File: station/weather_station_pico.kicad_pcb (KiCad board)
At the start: 2 copper layers, 60.2 x 74.1 mm, 26 parts, among them J1 Conn_01x03, J2 1984617, J3 STEMMA, J4 STEMMA_QT, J5 DS18B20, J6 1X7_HEADER, J7 73412-0110, J8 RJ11, J9 RJ11, U1 PICO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

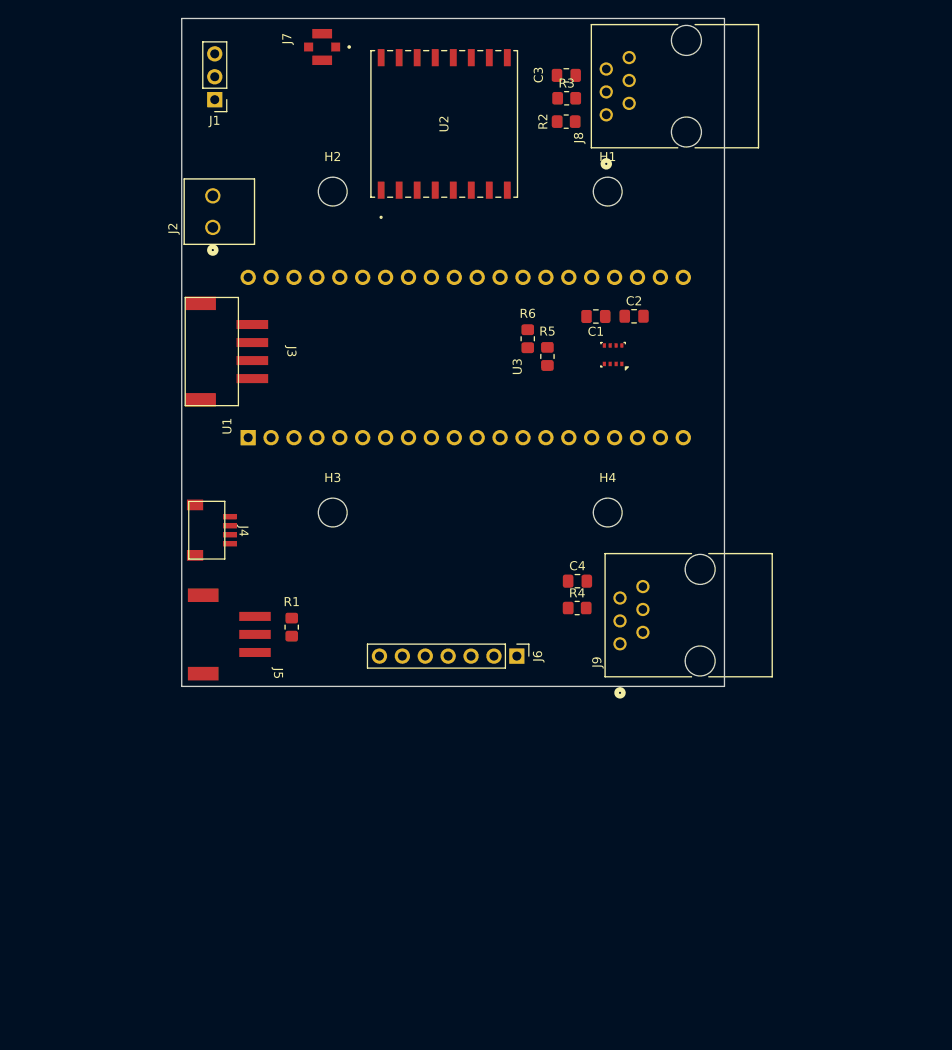
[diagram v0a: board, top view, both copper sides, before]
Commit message: Updated the weather stations components
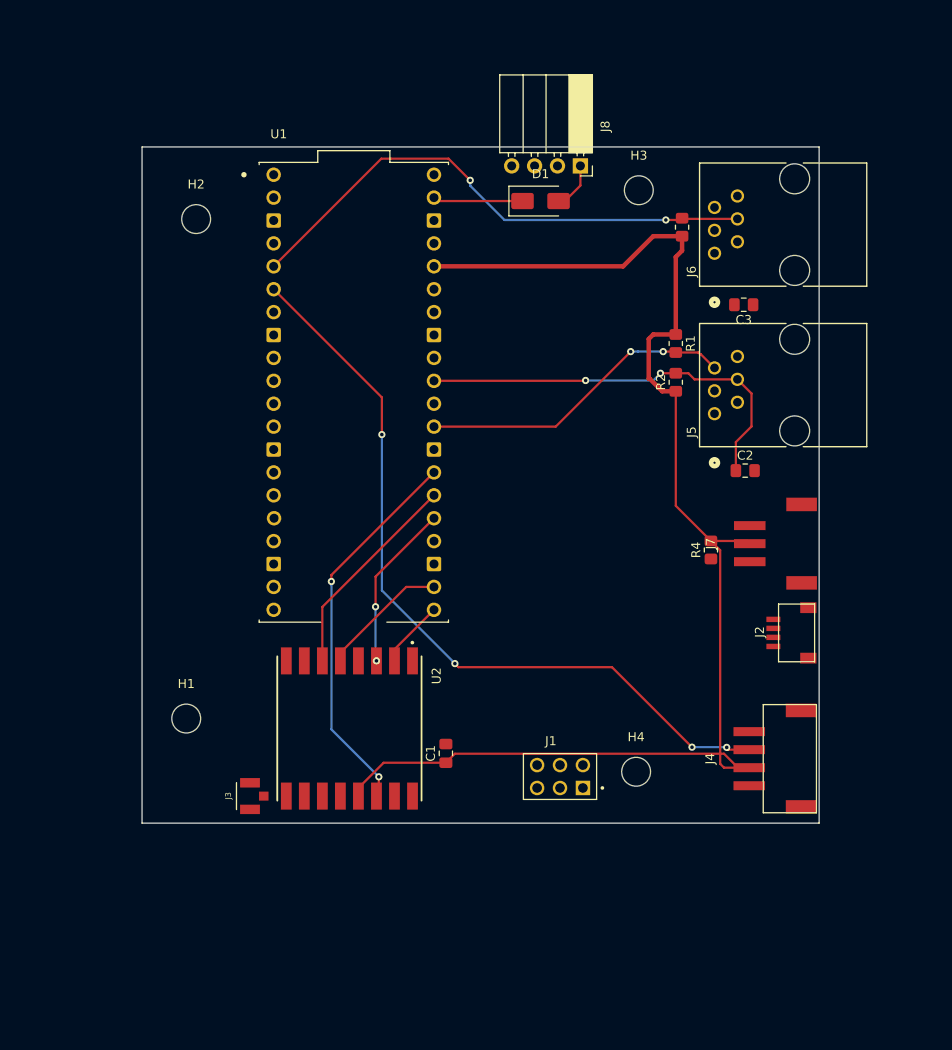
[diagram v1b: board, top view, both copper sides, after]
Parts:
- removed C4: 10pF, Capacitor_SMD:C_0805_2012Metric_Pad1.18x1.45mm_HandSolder
- removed J9: RJ11, WeatherStation:CONN6_5555165-1_TEC
- removed R5, R6: 4.7K, Resistor_SMD:R_0805_2012Metric_Pad1.20x1.40mm_HandSolder
- removed U3: BME280, Package_LGA:Bosch_LGA-8_2.5x2.5mm_P0.65mm_ClockwisePinNumbering
- added D1: SS12, Diode_SMD:D_SMA, F.Cu at (154.6, 65.5)
- C1: value 100nF -> 10uF
- C2: value 100nF -> 10pF
- J1: value Conn_01x03 -> DebugHeader; footprint Connector_PinHeader_2.54mm:PinHeader_1x03_P2.54mm_Vertical -> WeatherStation:DebugHeader
- J2: value 1984617 -> STEMMA_QT; footprint WeatherStation:CONN_1984617_PXC -> WeatherStation:STEMMA_SMALL
- J3: value STEMMA -> 73412-0110; footprint WeatherStation:STEMMA_LARGE -> WeatherStation:Antenna
- J4: value STEMMA_QT -> STEMMA; footprint WeatherStation:STEMMA_SMALL -> WeatherStation:STEMMA_LARGE
- J5: value DS18B20 -> RJ11; footprint WeatherStation:STEMMA_LARGE_3pin -> WeatherStation:CONN6_5555165-1_TEC
- J6: value 1X7_HEADER -> RJ11; footprint Connector_PinHeader_2.54mm:PinHeader_1x07_P2.54mm_Vertical -> WeatherStation:CONN6_5555165-1_TEC
- J7: value 73412-0110 -> DS18B20; footprint 734120110:MOLEX_73412-0110 -> WeatherStation:STEMMA_LARGE_3pin
- J8: value RJ11 -> Conn_01x04; footprint WeatherStation:CONN6_5555165-1_TEC -> Connector_PinSocket_2.54mm:PinSocket_1x04_P2.54mm_Horizontal
- R1: value R -> 10K
- R4: value 10K -> 4.7k
- U1: value PICO -> Pico; footprint WeatherStation:PinHeader_2x20_P2.54mm_Vertical -> WeatherStation:MODULE_SC918_PINS
- U2: footprint RFM69:RFM69HCW_SPK -> WeatherStation:RFM69
- moved J1 84.3 mm to (156.8, 129.3), turned to 0 degrees
- moved J2 77.4 mm to (181.2, 113.4)
- moved H1 74.8 mm to (115.3, 122.9)
- moved J7 73.8 mm to (179.6, 103.5)
- moved U2 67.9 mm to (133.4, 124.0), turned to -90 degrees
- moved J4 65.2 mm to (179.5, 127.3), turned to 90 degrees
- moved J5 58.1 mm to (173.9, 89.1), turned to 90 degrees
- moved R1 53.0 mm to (169.6, 81.3)
- moved C1 51.2 mm to (144.1, 126.8), turned to 90 degrees
- moved J6 49.8 mm to (173.9, 71.3), turned to 90 degrees
- moved J3 49.3 mm to (122.4, 131.5), turned to 90 degrees
- moved H3 49.3 mm to (165.5, 64.3)
- moved C3 32.2 mm to (177.1, 77.0)
- moved R2 31.4 mm to (169.6, 85.6), turned to 90 degrees
- moved H4 28.9 mm to (165.2, 128.8)
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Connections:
- net /RFM69_CS renamed /RFM69 Radio/RFM69_CS
- net /RFM69_RESET renamed /RFM69 Radio/RFM69_RESET
- net /SPI0_CLK renamed /RFM69 Radio/RFM69_CLK
- net /SPI0_MISO renamed /RFM69 Radio/RFM69_MISO
- net /SPI0_MOSI renamed /RFM69 Radio/RFM69_MOSI
- net /UART_TX renamed /UART0_TX
- C1 pad 1: VCC -> +3.3V
- C2 pad 1: VCC -> /WINDSPEED_TGR
- C3 pad 1: /WINDSPEED_TGR -> /RAIN_COUNT
- J1 pad 2: /UART_RX -> /SWCLK
- J1 pad 3: GND -> /UART0_RX
- J2 pad 2: +5V -> +3.3V
- J3 pad 1: GND -> Net-(U2-ANT)
- J3 pad 2: VCC -> GND
- J3 pad 3: /SDA -> (no net)
- J4 pad 2: VCC -> +3.3V
- J4 pad 3: /SDA -> /I2C0_SDA
- J4 pad 4: /SCL -> /I2C0_SCL
- J5 pad 1: /ONE_WIRE -> unconnected-(J5-Pad1)
- J5 pad 2: VCC -> GND
- J5 pad 4: (no net) -> /WINDSPEED_TGR
- J5 pad 5: (no net) -> /WINDDIR_OUT
- J6 pad 1: /MOSI -> unconnected-(J6-Pad1)
- J6 pad 2: /MISO -> unconnected-(J6-Pad2)
- J6 pad 3: /SCK -> GND
- J6 pad 4: /~{CS} -> /RAIN_COUNT
- J6 pad 5: /LIGHTNING_INT -> unconnected-(J6-Pad5)
- J6 pad 6: VCC -> unconnected-(J6-Pad6)
- J7 pad 1: Net-(U2-ANT) -> /ONE_WIRE
- J7 pad 2: GND -> +3.3V
- J7 pad 3: (no net) -> GND
- J8 pad 1: unconnected-(J8-Pad1) -> /Battery Charger/VOUT
- J8 pad 2: GND -> /Battery Charger/SET
- J8 pad 3: GND -> /Battery Charger/~{FAULT}
- J8 pad 4: /WINDSPEED_TGR -> /Battery Charger/~{CHRG}
- R1 pad 1: /ONE_WIRE -> +3.3V
- R1 pad 2: VCC -> /WINDDIR_OUT
- R2 pad 1: VCC -> +3.3V
- R2 pad 2: /WINDDIR_OUT -> /WINDSPEED_TGR
- R3 pad 1: VCC -> +3.3V
- R3 pad 2: /WINDSPEED_TGR -> /RAIN_COUNT
- R4 pad 1: VCC -> /ONE_WIRE
- R4 pad 2: /RAIN_COUNT -> +3.3V
- U1 pad 16: /SDA -> unconnected-(U1-GP12-Pad16)
- U1 pad 17: /SCL -> unconnected-(U1-GP13-Pad17)
- U1 pad 2: /UART_RX -> /UART0_RX
- U1 pad 20: /ONE_WIRE -> unconnected-(U1-GP15-Pad20)
- U1 pad 27: /FRM69_INTR -> /RFM69 Radio/RFM69_INTR
- U1 pad 29: /WINDSPEED_TGR -> /WINDDIR_OUT
- U1 pad 31: /WINDDIR_OUT -> /WINDSPEED_TGR
- U1 pad 36: VCC -> +3.3V
- U1 pad 39: +5V -> Net-(D1-K)
- U1 pad 5: unconnected-(U1-GP3-Pad5) -> /RAIN_COUNT
- U1 pad 6: /RAIN_COUNT -> /I2C0_SDA
- U1 pad 7: unconnected-(U1-GP5-Pad7) -> /I2C0_SCL
- U2 pad 13: VCC -> +3.3V
- U2 pad 14: /RFM69_INTR -> /RFM69 Radio/RFM69_INTR
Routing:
- net +3.3V: track 0.00 -> 148.9 mm
- net /I2C0_SDA: track 0.00 -> 86.5 mm, vias 0 -> 4
- net /RAIN_COUNT: track 0.00 -> 59.7 mm, vias 0 -> 2
- net /WINDSPEED_TGR: track 0.00 -> 45.8 mm, vias 0 -> 2
- net /RFM69 Radio/RFM69_INTR: track 0.00 -> 42.9 mm, vias 0 -> 2
- net /WINDDIR_OUT: track 0.00 -> 35.3 mm, vias 0 -> 2
- net /RFM69 Radio/RFM69_RESET: track 0.00 -> 23.5 mm
- net /RFM69 Radio/RFM69_MOSI: track 0.00 -> 18.5 mm, vias 0 -> 2
- net /RFM69 Radio/RFM69_CS: track 0.00 -> 14.3 mm
- net Net-(D1-K): track 0.00 -> 9.98 mm
- net /RFM69 Radio/RFM69_MISO: track 0.00 -> 7.47 mm
- net /Battery Charger/VOUT: track 0.00 -> 5.31 mm
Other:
- board size 60.2 x 74.1 mm -> 75.1 x 75 mm

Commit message: Signed-off-by: Scott Perkins <whatisbyandby@gmail.com>
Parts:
- J8: value Conn_01x04 -> Battery Charger; footprint Connector_PinSocket_2.54mm:PinSocket_1x04_P2.54mm_Horizontal -> Connector_PinSocket_2.54mm:PinSocket_2x03_P2.54mm_Vertical
- U1: footprint WeatherStation:MODULE_SC918_PINS -> WeatherStation:Pico_SMD_Headers; moved to B.Cu
- moved H3 63.9 mm to (117.2, 106.2)
- moved H1 58.5 mm to (117.3, 64.4)
- moved H2 42.9 mm to (159.1, 64.3)
- moved H4 23.6 mm to (159.1, 106.0)
- moved J8 9.14 mm to (166.6, 66.7), turned to 180 degrees
- moved J3 9.12 mm to (113.7, 128.8)
- moved U2 8.70 mm to (124.7, 124.1)
- moved C1 8.70 mm to (135.4, 126.8)
- moved R3 5.63 mm to (170.1, 74.0)
- moved D1 4.49 mm to (155.0, 70.0)
- moved U1 4.44 mm to (138.0, 88.3), turned to 180 degrees
- moved J4 4.30 mm to (179.4, 123.0)
- moved J7 3.04 mm to (179.6, 100.5)
- moved C2 2.84 mm to (177.7, 92.6)
- moved R4 2.60 mm to (173.6, 101.6)
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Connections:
- net /Battery Charger/VOUT renamed /Battery Charger/Load+
- J8 pad 2: /Battery Charger/SET -> GND
- J8 pad 3: /Battery Charger/~{FAULT} -> GND
- J8 pad 4: /Battery Charger/~{CHRG} -> /Battery Charger/SET
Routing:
- net /I2C0_SDA: track 86.5 -> 0.00 mm, vias 4 -> 0
- net /RAIN_COUNT: track 59.7 -> 0.00 mm, vias 2 -> 0
- net /WINDSPEED_TGR: track 45.8 -> 0.00 mm, vias 2 -> 0
- net /RFM69 Radio/RFM69_INTR: track 42.9 -> 0.00 mm, vias 2 -> 0
- net /WINDDIR_OUT: track 35.3 -> 0.00 mm, vias 2 -> 0
- net /RFM69 Radio/RFM69_RESET: track 23.5 -> 0.00 mm
- net /RFM69 Radio/RFM69_MOSI: track 18.5 -> 0.00 mm, vias 2 -> 0
- net /RFM69 Radio/RFM69_CS: track 14.3 -> 0.00 mm
- net +3.3V: track 148.9 -> 163.0 mm, vias 0 -> 2
- net /RFM69 Radio/RFM69_MISO: track 7.47 -> 0.00 mm
- net Net-(U2-ANT): track 0.00 -> 5.01 mm
- net Net-(D1-K): track 9.98 -> 7.82 mm, vias 0 -> 1
- net /Battery Charger/Load+: track 5.31 -> 6.35 mm

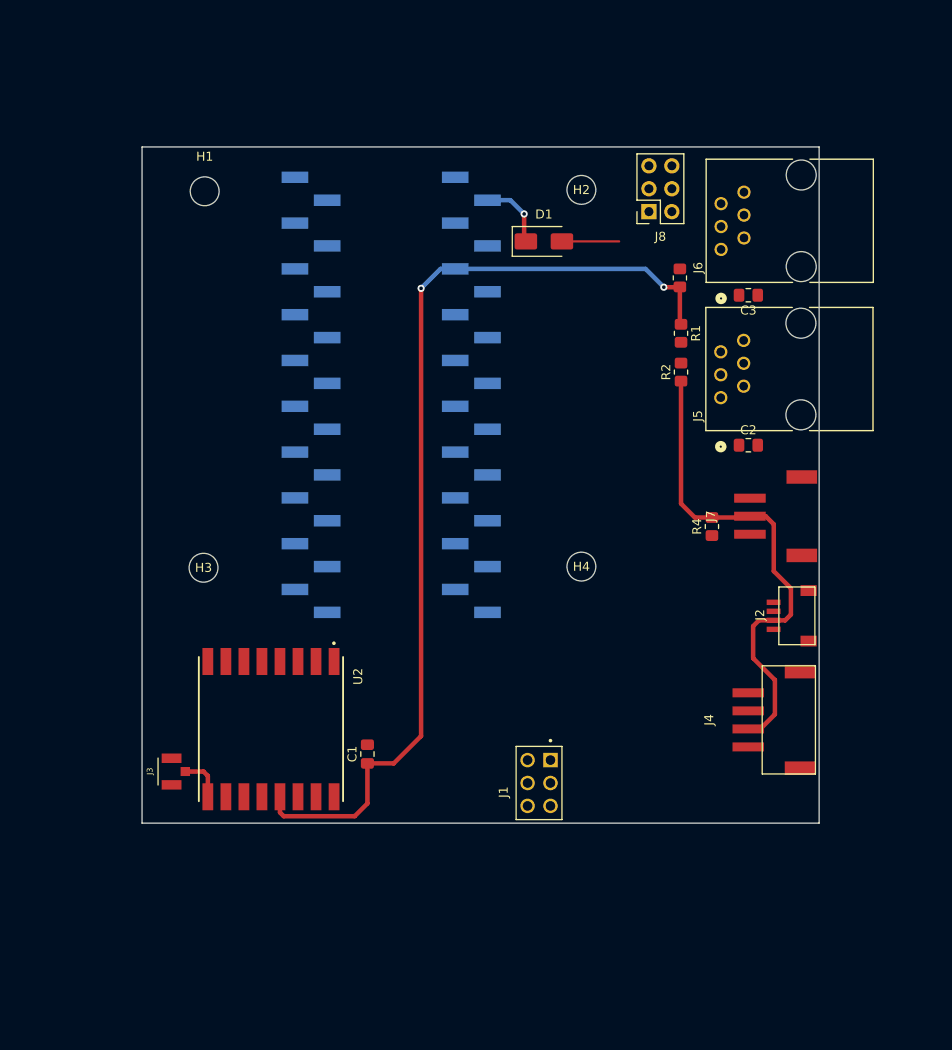
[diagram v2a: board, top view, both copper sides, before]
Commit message: Reworked layout
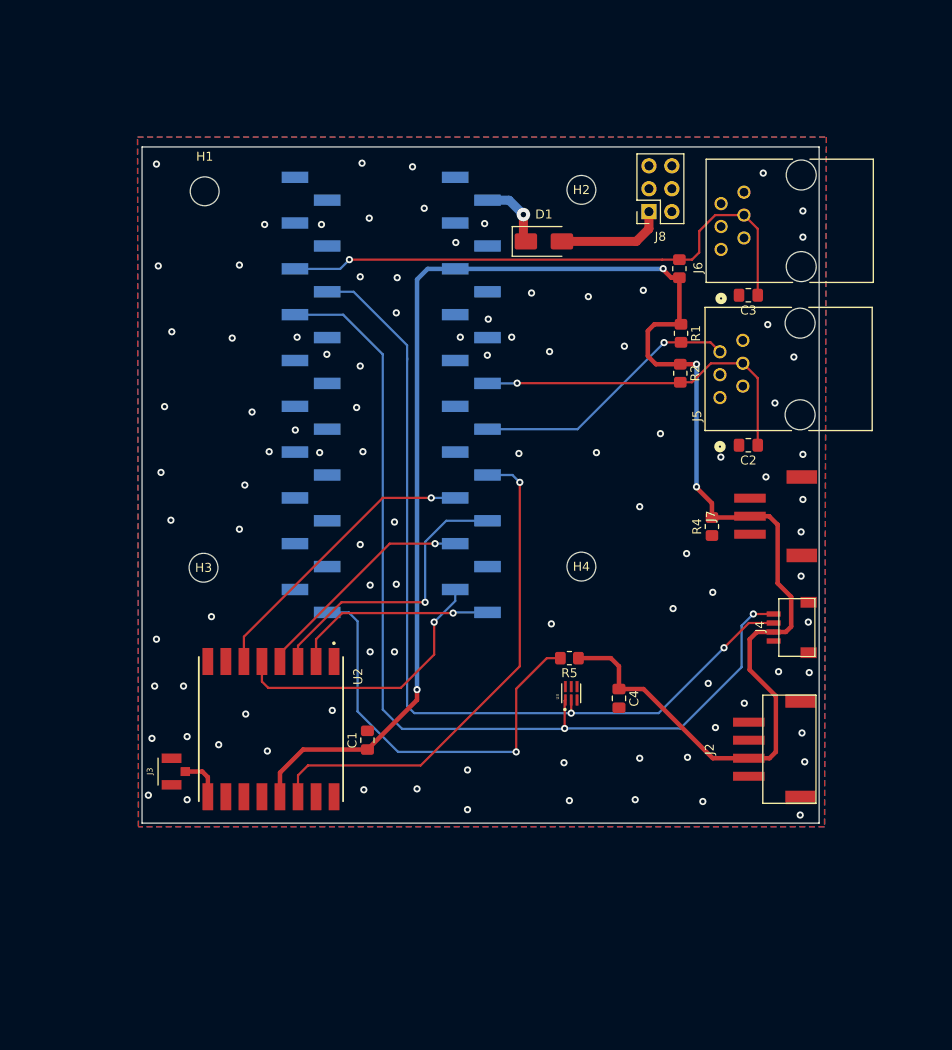
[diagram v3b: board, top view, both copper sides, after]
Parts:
- removed J1: DebugHeader, WeatherStation:DebugHeader
- added C4: 1uF, Capacitor_SMD:C_0805_2012Metric_Pad1.18x1.45mm_HandSolder, F.Cu at (163.3, 120.7)
- added R5: 10k, Resistor_SMD:R_0805_2012Metric_Pad1.20x1.40mm_HandSolder, F.Cu at (157.8, 116.2)
- added U3: APDS_LightSensor, WeatherStation:APDS_LIGHT_SENSOR, F.Cu at (158.0, 120.1)
- J2: footprint WeatherStation:STEMMA_SMALL -> WeatherStation:STEMMA_LARGE
- J4: footprint WeatherStation:STEMMA_LARGE -> WeatherStation:STEMMA_SMALL
- moved J2 14.9 mm to (179.4, 126.3)
- moved J4 10.4 mm to (181.2, 112.8)
- moved C1 1.53 mm to (135.4, 125.3)
- moved R3 1.03 mm to (170.0, 73.0)
- moved R2 0.15 mm to (170.1, 84.6), turned to -90 degrees
- moved J5 0.09 mm to (174.5, 87.3)
- turned C2 to 180 degrees
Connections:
- J2 pad 5: (no net) -> GND
- J2 pad 6: (no net) -> GND
- J3 pad 3: (no net) -> GND
- J4 pad 5: (no net) -> GND
- J4 pad 6: (no net) -> GND
- J7 pad 4: (no net) -> GND
- J7 pad 5: (no net) -> GND
- U1 pad 1: /UART0_TX -> unconnected-(U1-GP0-Pad1)
- U1 pad 2: /UART0_RX -> unconnected-(U1-GP1-Pad2)
- U1 pad 20: unconnected-(U1-GP15-Pad20) -> /LIGHT_INTR
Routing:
- net /I2C0_SCL: track 0.00 -> 106.4 mm, vias 0 -> 2
- net /I2C0_SDA: track 0.00 -> 98.2 mm, vias 0 -> 2
- net /RAIN_COUNT: track 0.00 -> 63.3 mm, vias 0 -> 1
- net /RFM69 Radio/RFM69_INTR: track 0.00 -> 56.3 mm, vias 0 -> 1
- net /LIGHT_INTR: track 0.00 -> 46.5 mm, vias 0 -> 1
- net /WINDSPEED_TGR: track 0.00 -> 39.0 mm, vias 0 -> 1
- net +3.3V: track 163.0 -> 200.3 mm, vias 2 -> 4
- net /RFM69 Radio/RFM69_RESET: track 0.00 -> 32.6 mm, vias 0 -> 1
- net /RFM69 Radio/RFM69_MOSI: track 0.00 -> 32.4 mm, vias 0 -> 1
- net /RFM69 Radio/RFM69_CS: track 0.00 -> 31.9 mm, vias 0 -> 1
- net /WINDDIR_OUT: track 0.00 -> 30.2 mm, vias 0 -> 1
- net /RFM69 Radio/RFM69_CLK: track 0.00 -> 25.4 mm, vias 0 -> 1
- net /RFM69 Radio/RFM69_MISO: track 0.00 -> 22.7 mm, vias 0 -> 1
- net /Battery Charger/Load+: track 6.35 -> 12.1 mm
- net GND: vias 0 -> 96
- added copper zone on B.Cu, net GND
- added copper zone on F.Cu, net GND
